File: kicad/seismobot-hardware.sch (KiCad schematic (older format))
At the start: 66 parts

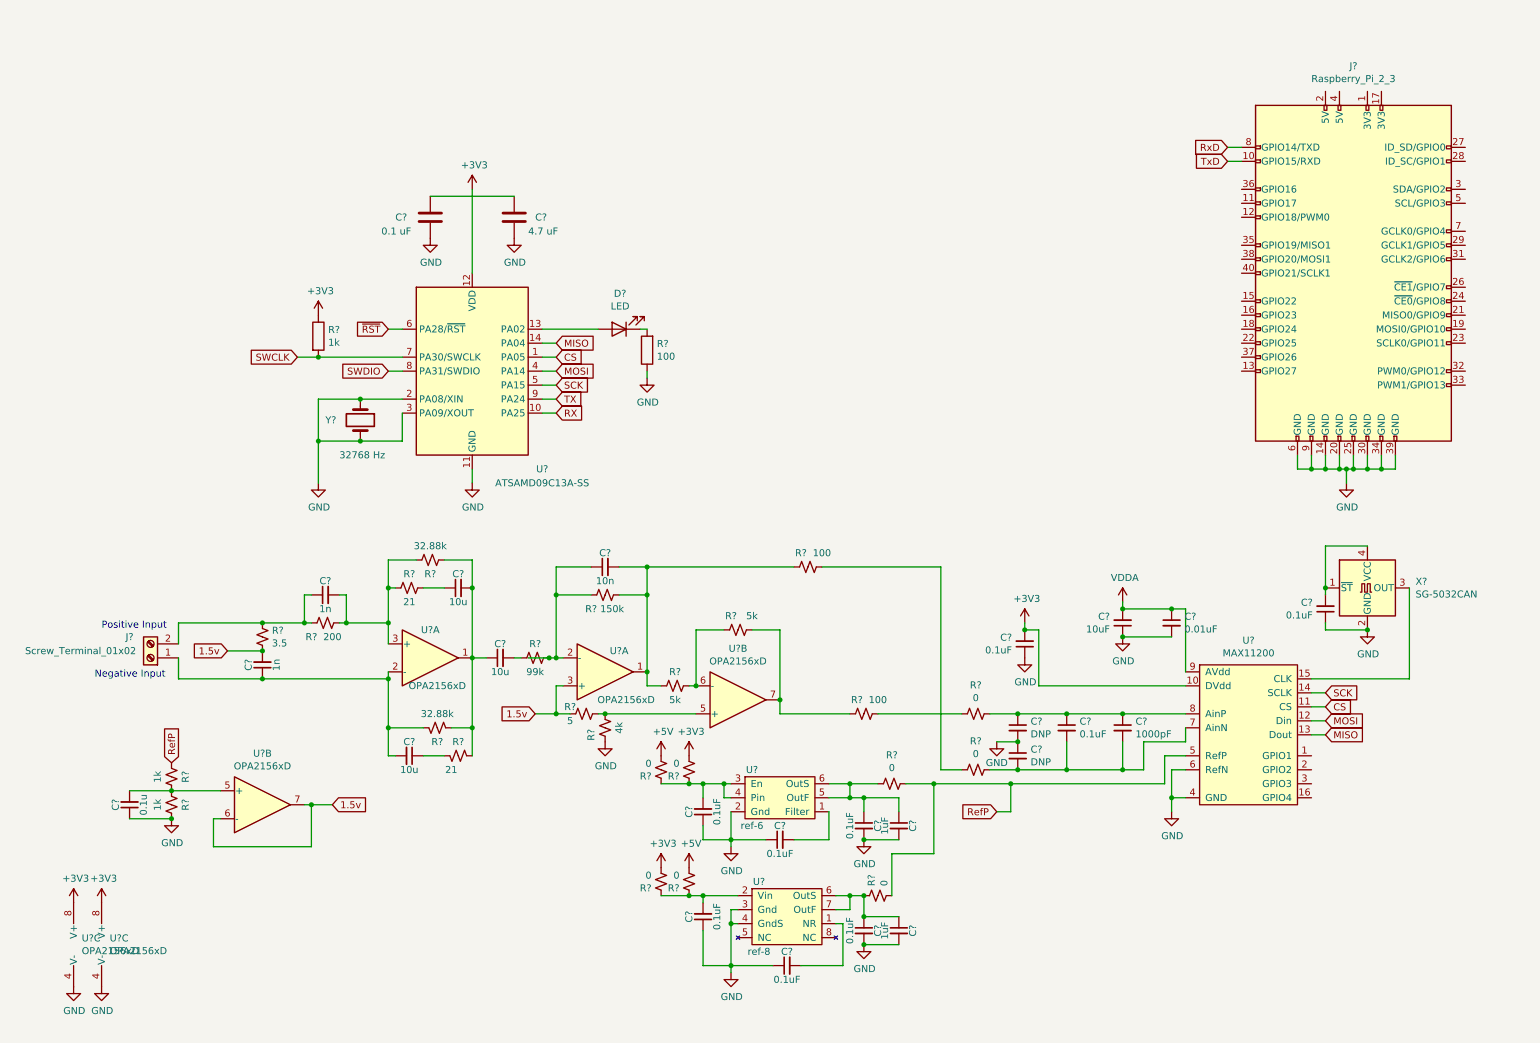
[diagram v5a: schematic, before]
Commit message: Cleaned things up, add new signal path
added a new 6-pole, 2-zero filter
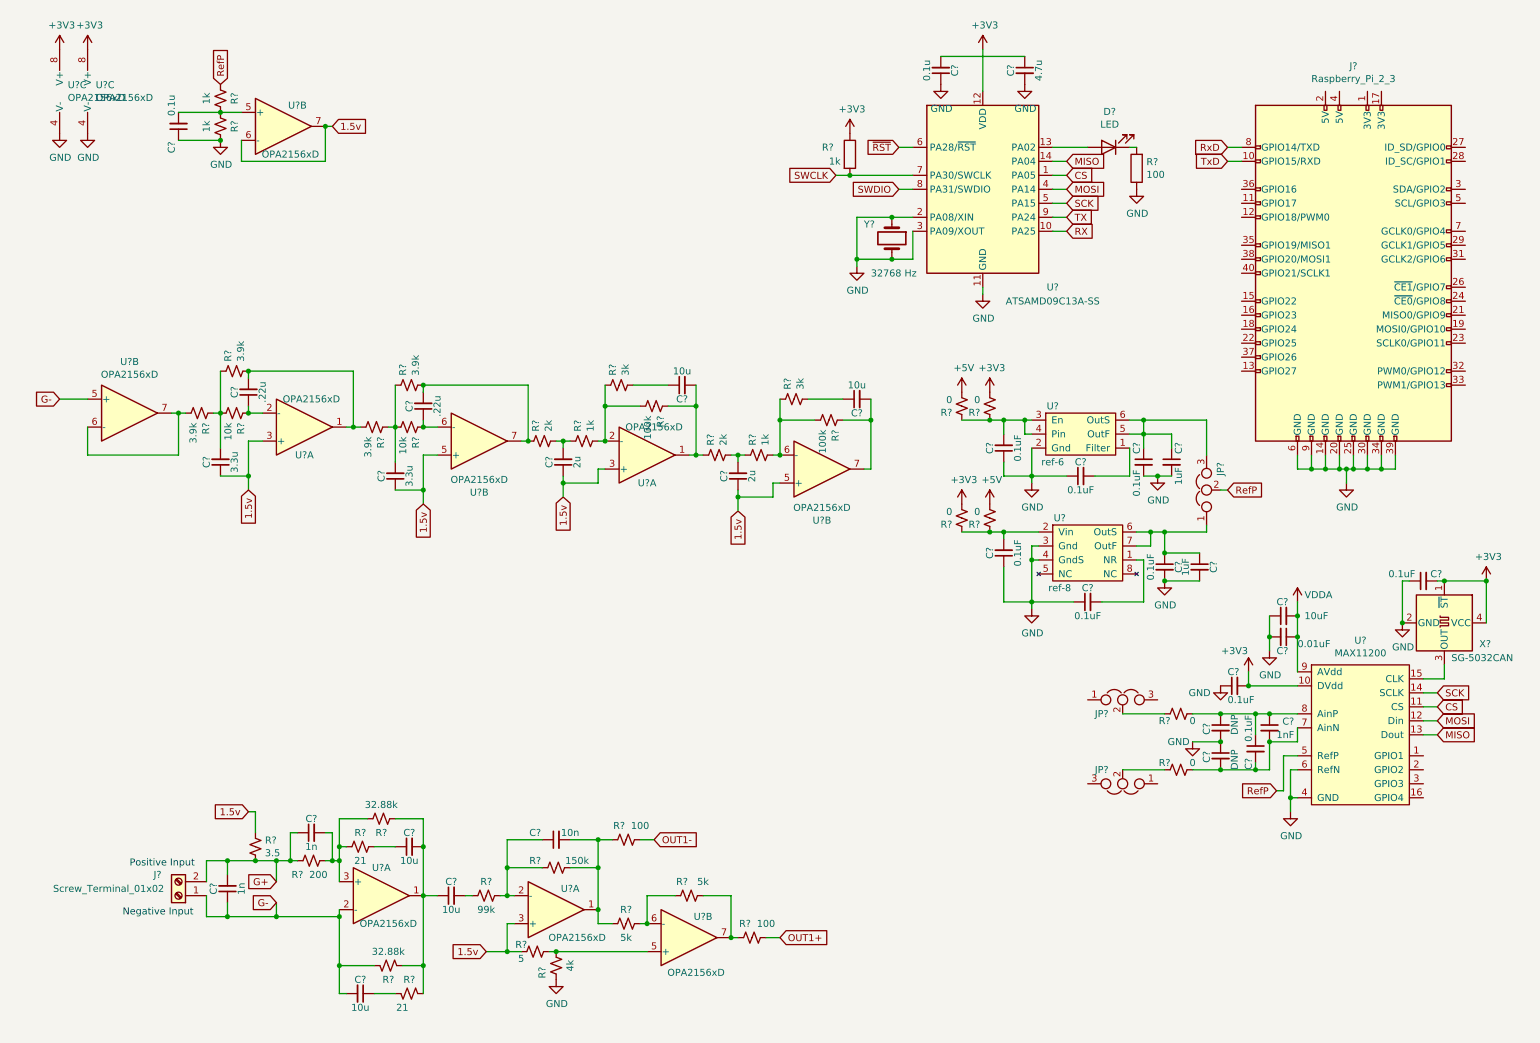
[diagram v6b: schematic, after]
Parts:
- removed C?: 4.7 uF, symbol Device:C
- removed C?: 0.1 uF, symbol Device:C
- removed R? (x2): 0, symbol Device:R_Small_US
- added C? (x2): .22u, symbol Device:C_Small
- added C? (x2): 3.3u, symbol Device:C_Small
- added C? (x2): 2u, symbol Device:C_Small
- added C? (x2): 10u, symbol Device:C_Small
- added C?: 0.1u, symbol Device:C_Small
- added C?: 4.7u, symbol Device:C_Small
- added JP? (x3): Jumper_NC_Dual, symbol Device:Jumper_NC_Dual
- added R? (x4): 3.9k, symbol Device:R_Small_US
- added R? (x2): 10k, symbol Device:R_Small_US
- added R? (x2): 2k, symbol Device:R_Small_US
- added R? (x2): 1k, symbol Device:R_Small_US
- added R? (x2): 100k, symbol Device:R_Small_US
- added R? (x2): 3k, symbol Device:R_Small_US
- added U? (x5): OPA2156xD, Package_SO:SOIC-8_3.9x4.9mm_P1.27mm, symbol Amplifier_Operational:OPA2156xD
- C?: value 1000pF -> 1nF
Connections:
- net +3V3: now also C?.2, X?.1 (~ST), X?.4 (VCC)
- net 1.5v: now also R?.1, C?.1, C?.1, C?.1, C?.1, U?.3 (+), U?.3 (+), U?.5 (+), U?.5 (+); no longer C?.2, R?.2
- net GND: now also C?.1, C?.2
- net RefP: now also JP?.2
- net at R?.2: now also JP?.2; no longer R?.1 (x2)
- net at C?.1, C?.1, U?.5 (OutF)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: now also JP?.3
- net at C?.1, C?.1, U?.6 (OutS)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: now also JP?.1
- net G-: now reaches C?.1, C?.2, J?.1 (Pin_1), R?.1, U?.2 (-)
- net G-: now also U?.5 (+)
- net G+: now reaches C?.1, J?.2 (Pin_2), R?.2
- net G+: now also C?.2, R?.2; no longer R?.1
- new net: R?.2, U?.6 (-), U?.7
- new net: C?.2, R?.2, R?.2, U?.1
- new net: C?.1, R?.1, U?.2 (-)
- new net: C?.2, R?.1, R?.1, R?.2 (x2)
- new net: C?.2, R?.1, R?.2, U?.7
- new net: C?.2, R?.1, R?.2 (x2)
- new net: R?.1, R?.2, R?.2, U?.2 (-)
- new net: C?.2, R?.1, R?.1, U?.1
- new net: C?.1, R?.2 (x2)
- new net: C?.1, R?.1, U?.6 (-)
- new net: R?.1, R?.2, R?.2, U?.6 (-)
- new net: C?.2, R?.1, U?.7
- new net: C?.1, C?.2
- new net OUT1+: R?.1
- new net OUT1-: R?.1
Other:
- moved on the sheet: C?, D?, J?, R?, U?, U?A, U?B, U?C, X?, Y?

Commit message: add jumpers for signal path selection
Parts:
- added JP? (x2): Jumper_NC_Dual, symbol Device:Jumper_NC_Dual
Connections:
- net OUT1+ is gone; now on net OUTa+: R?.1
- net OUT1- is gone; now on net OUTa-: R?.1
- net 1.5v: now also JP?.1
- net OUTa+: now reaches JP?.1
- net OUTa-: now reaches JP?.3
- net G+ renamed Ga+
- net Ga+: now also JP?.3; no longer J?.2 (Pin_2)
- net G- renamed Ga-
- net Ga-: now also JP?.3; no longer J?.1 (Pin_1), U?.5 (+)
- new net: J?.1 (Pin_1), JP?.2
- new net: J?.2 (Pin_2), JP?.2
- new net Gb+: JP?.1, U?.5 (+)
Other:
- moved on the sheet: C?, J?, R?, U?A, U?B

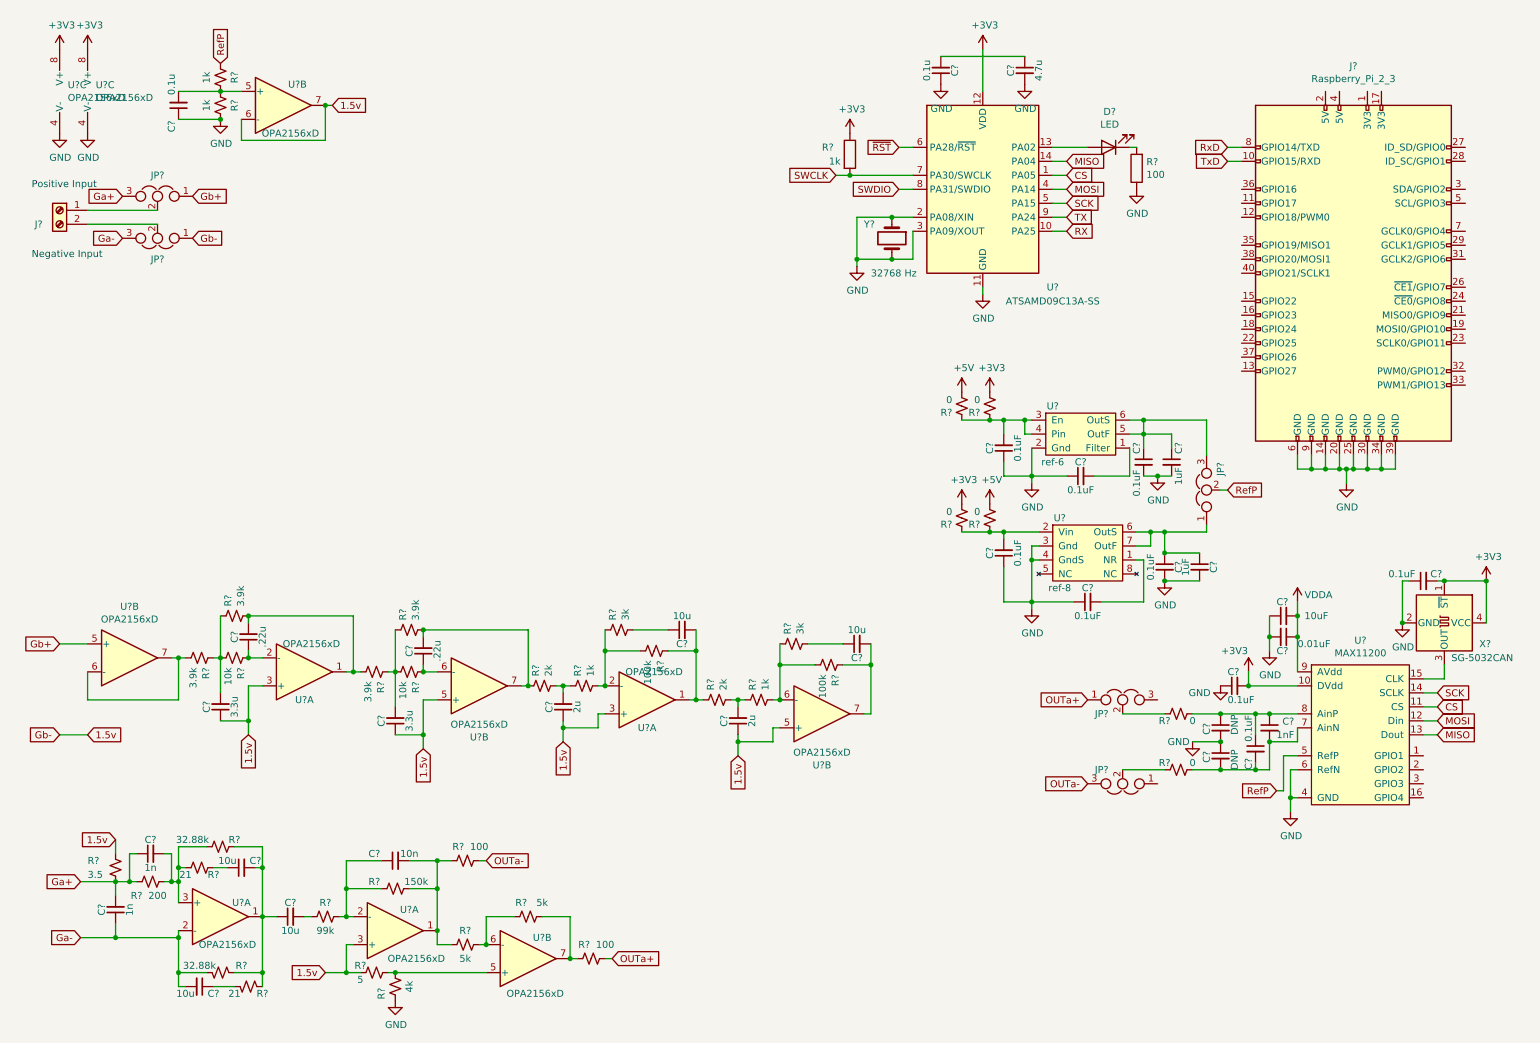
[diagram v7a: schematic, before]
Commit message: add footprints to all components
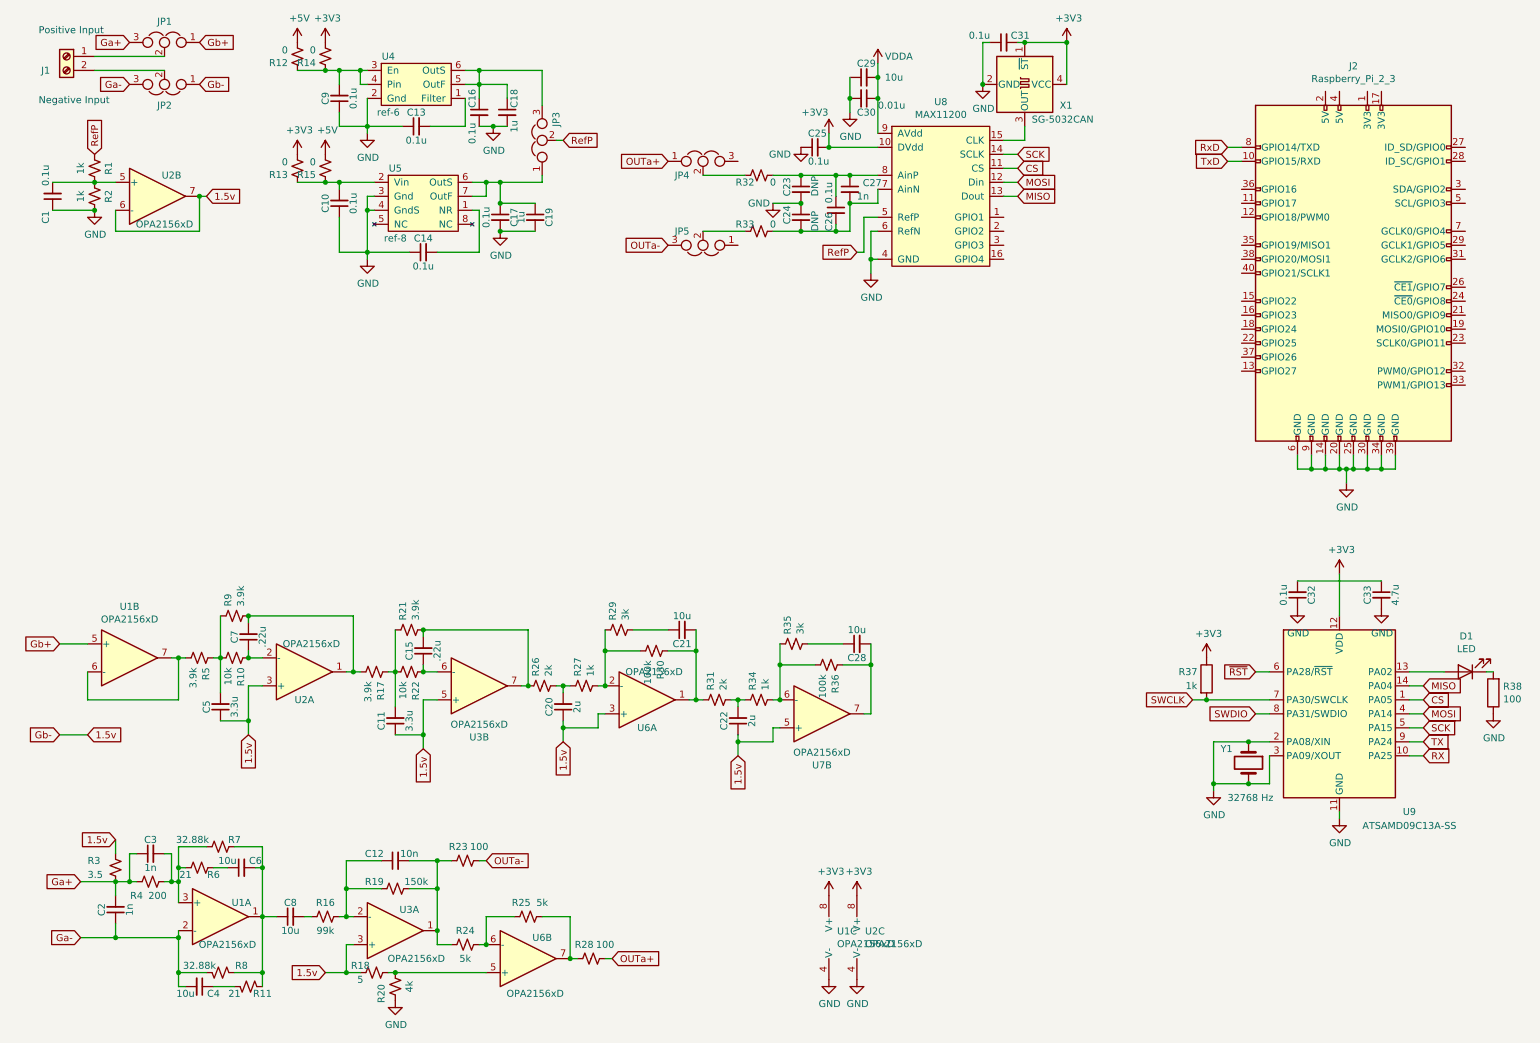
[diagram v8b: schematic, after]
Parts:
- C1, C11, C12, C15, C2, C20, C22, C23, C24, C3, C32, C33, C5, C7: renamed from C?; footprint (none) -> Capacitor_SMD:C_0805_2012Metric
- C10, C13, C14, C16, C17, C25, C26, C31, C9: renamed from C?; value 0.1uF -> 0.1u; footprint (none) -> Capacitor_SMD:C_0805_2012Metric
- C18, C19: renamed from C?; value 1uF -> 1u; footprint (none) -> Capacitor_SMD:C_0805_2012Metric
- C21, C28, C4, C6, C8: renamed from C?; footprint (none) -> Capacitor_SMD:C_1206_3216Metric
- C27: renamed from C?; value 1nF -> 1n; footprint (none) -> Capacitor_SMD:C_0805_2012Metric
- C29: renamed from C?; value 10uF -> 10u; footprint (none) -> Capacitor_SMD:C_1206_3216Metric
- C30: renamed from C?; value 0.01uF -> 0.01u; footprint (none) -> Capacitor_SMD:C_0805_2012Metric
- D1: renamed from D?; footprint (none) -> LED_SMD:LED_0805_2012Metric
- J1: renamed from J?; footprint (none) -> Connector_Phoenix_MC:PhoenixContact_MCV_1,5_2-G-3.5_1x02_P3.50mm_Vertical
- J2: renamed from J?; footprint (none) -> Connector_PinHeader_2.54mm:PinHeader_2x20_P2.54mm_Vertical
- JP1, JP2, JP3, JP4, JP5: renamed from JP?; footprint (none) -> Connector_PinHeader_2.54mm:PinHeader_1x03_P2.54mm_Vertical
- R1, R10, R11, R12, R13, R14, R15, R16, R17, R18, R19, R2, R20, R21, R22, R23, R24, R25, R26, R27, R28, R29, R3, R30, R31, R32, R33, R34, R35, R36, R37, R38, R4, R5, R6, R7, R8, R9: renamed from R?; footprint (none) -> Resistor_SMD:R_0805_2012Metric
- U4: renamed from U?; footprint (none) -> Package_TO_SOT_SMD:SOT-23-6
- U5: renamed from U?; footprint (none) -> Package_SO:SOIC-8_3.9x4.9mm_P1.27mm
- Y1: renamed from Y?; footprint (none) -> Crystal:Crystal_SMD_EuroQuartz_EQ161-2Pin_3.2x1.5mm
- gave numbers to parts that had none: 8
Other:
- moved on the sheet: C1, C10, C13, C14, C16, C17, C18, C19, C23, C24, C25, C26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
